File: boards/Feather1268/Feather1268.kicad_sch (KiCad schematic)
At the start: 22 parts, among them J2 USB4105-GF-A, J4 Conn_01x03, U2 ESP32-S3-MINI-1U, U3 ECMF02-2AMX6, U5 AMS1117-3.3

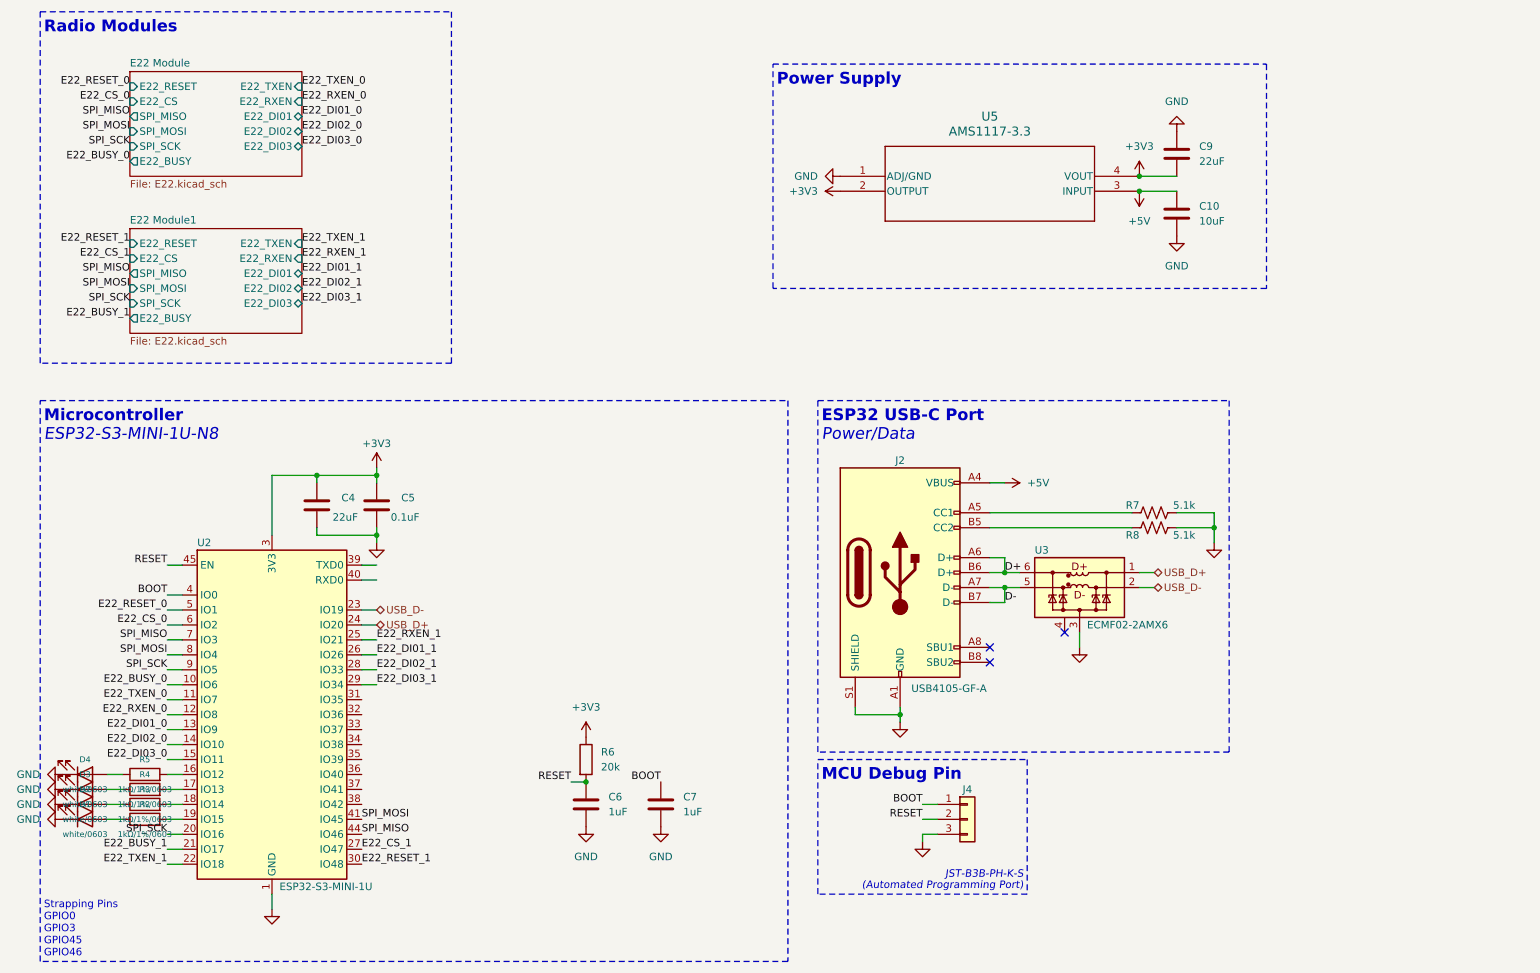
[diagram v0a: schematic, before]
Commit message: made some sch formatting / libs / routing changes
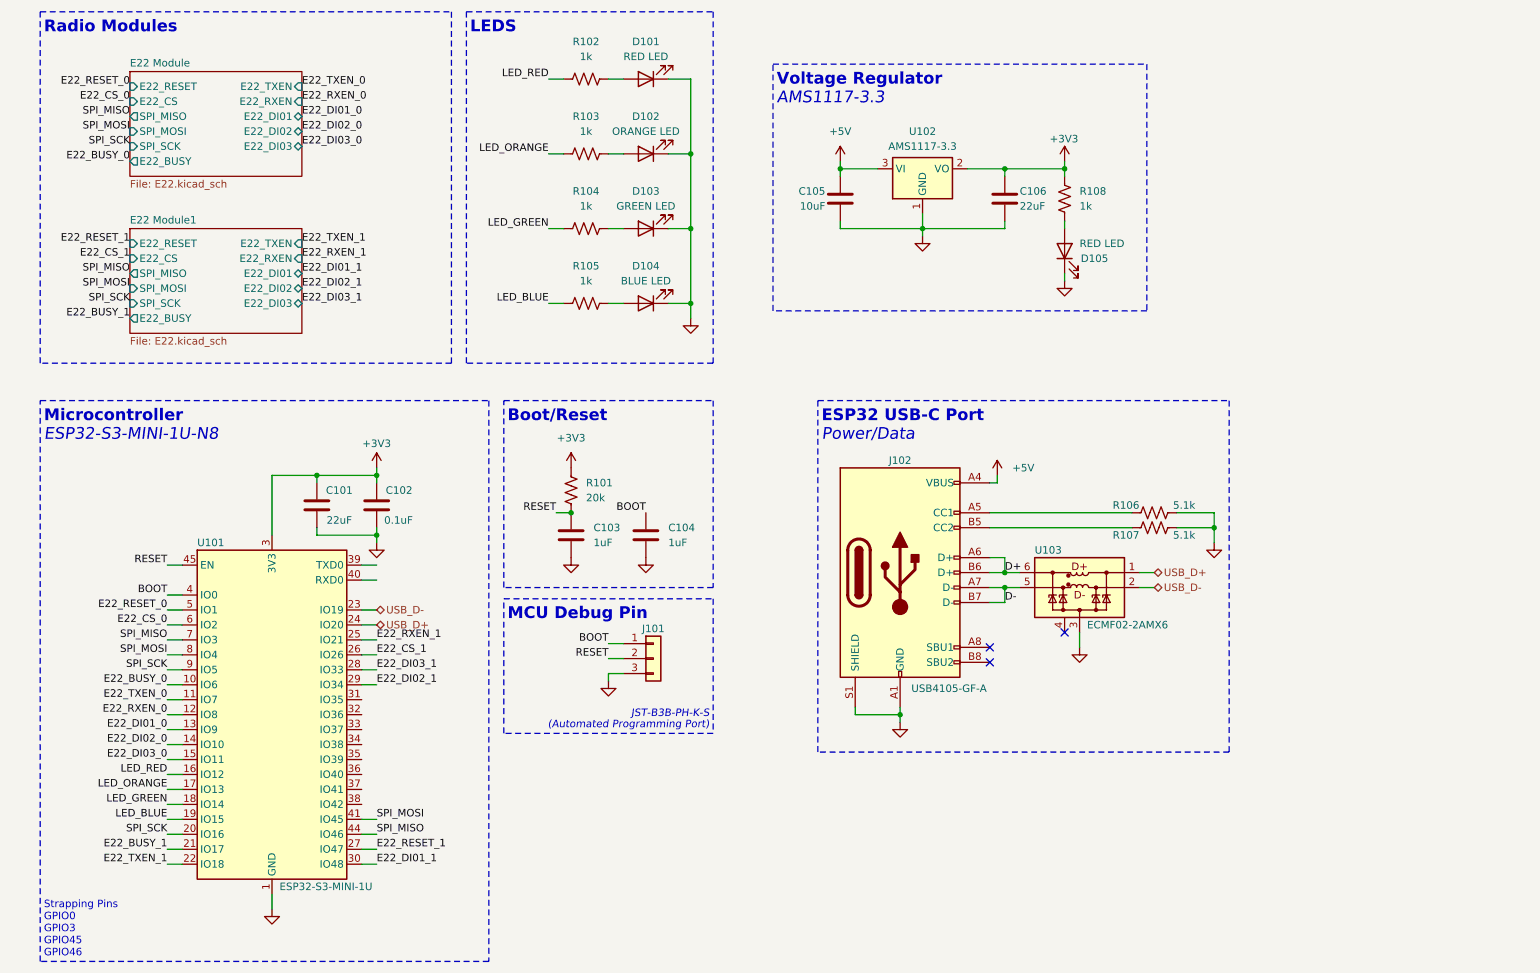
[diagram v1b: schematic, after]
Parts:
- removed C10: 10uF, Capacitor_SMD:C_0603_1608Metric, symbol Device:C
- removed C6, C7: 1uF, Capacitor_SMD:C_0603_1608Metric, symbol Device:C
- removed C9: 22uF, Capacitor_SMD:C_0603_1608Metric, symbol Device:C
- removed D1, D2, D3, D4: white/0603, LED_SMD:LED_0603_1608Metric, symbol Device:LED
- removed R2, R3, R4, R5: 1kΩ/1%/0603, Resistor_SMD:R_0603_1608Metric, symbol TMC2209-BOB-v1.0-rescue:R-Device
- removed R6: 20k, Resistor_SMD:R_0603_1608Metric, symbol Device:R
- removed U5: AMS1117-3.3, SOT_AMS1117-2.5_AMS, symbol AMS1117-3.3:AMS1117-3.3
- added C103, C104: 1uF, Capacitor_SMD:C_0603_1608Metric, symbol Device:C
- added C105: 10uF, Capacitor_SMD:C_0603_1608Metric, symbol Device:C
- added C106: 22uF, Capacitor_SMD:C_0603_1608Metric, symbol Device:C
- added D101, D105: RED LED, LED_SMD:LED_0603_1608Metric, symbol Device:LED
- added D102: ORANGE LED, LED_SMD:LED_0603_1608Metric, symbol Device:LED
- added D103: GREEN LED, LED_SMD:LED_0603_1608Metric, symbol Device:LED
- added D104: BLUE LED, LED_SMD:LED_0603_1608Metric, symbol Device:LED
- added R101: 20k, Resistor_SMD:R_0603_1608Metric, symbol Device:R_US
- added R102, R103, R104, R105, R108: 1k, Resistor_SMD:R_0603_1608Metric, symbol Device:R_US
- added U102: AMS1117-3.3, Package_TO_SOT_SMD:SOT-223-3_TabPin2, symbol Regulator_Linear:AMS1117-3.3
- renumbered C4 to C101, C5 to C102, J4 to J101, J2 to J102, R7 to R106, R8 to R107, U2 to U101, U3 to U103
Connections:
- net +3V3: now also C106.1, R101.1, R108.1, U102.2 (VO)
- net +5V: now also C105.1, U102.3 (VI)
- net BOOT: now also C104.1
- net E22_CS_1: now also U101.26 (IO26); no longer U101.27 (IO47)
- net E22_DI01_1: now also U101.30 (IO48); no longer U101.26 (IO26)
- net E22_DI02_1: now also U101.29 (IO34); no longer U101.28 (IO33)
- net E22_DI03_1: now also U101.28 (IO33); no longer U101.29 (IO34)
- net E22_RESET_1: now also U101.27 (IO47); no longer U101.30 (IO48)
- net GND: now also C103.2, C104.2, C105.2, C106.2, D101.1 (K), D102.1 (K), D103.1 (K), D104.1 (K), D105.1 (K), U102.1 (GND)
- net RESET: now also C103.1, R101.2
- net LED_GREEN: now reaches U101.18 (IO14)
- net LED_GREEN: now also R104.1
- net LED_RED: now reaches U101.16 (IO12)
- net LED_RED: now also R102.1
- net LED_ORANGE: now reaches U101.17 (IO13)
- net LED_ORANGE: now also R103.1
- net LED_BLUE: now reaches U101.19 (IO15)
- net LED_BLUE: now also R105.1
- new net: D105.2 (A), R108.2
- new net: D104.2 (A), R105.2
- new net: D102.2 (A), R103.2
- new net: D103.2 (A), R104.2
- new net: D101.2 (A), R102.2
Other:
- note added: "AMS1117-3.3"
- note added: "Boot/Reset"
- note added: "LEDS"
- note added: "Voltage Regulator"
- note removed: "Power Supply"
- moved on the sheet: J101

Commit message: done ish
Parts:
- added J1: Conn_01x02, Connector_PinHeader_2.54mm:PinHeader_1x02_P2.54mm_Vertical, symbol Connector_Generic:Conn_01x02
- added TP1, TP2, TP3, TP4, TP5, TP6: TestPoint_Small, TestPoint:TestPoint_Pad_D1.0mm, symbol Connector:TestPoint_Small
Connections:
- net E22_BUSY_1: now also U101.22 (IO18); no longer U101.21 (IO17)
- net E22_CS_0: now also U101.5 (IO1); no longer U101.6 (IO2)
- net E22_CS_1: now also U101.21 (IO17); no longer U101.26 (IO26)
- net E22_DI01_0: now also U101.9 (IO5); no longer U101.13 (IO9)
- net E22_DI02_0: now also U101.38 (IO42); no longer U101.14 (IO10)
- net E22_DI03_0: now also U101.41 (IO45); no longer U101.15 (IO11)
- net E22_RESET_0: now also U101.13 (IO9); no longer U101.5 (IO1)
- net E22_RXEN_0: now also U101.11 (IO7); no longer U101.12 (IO8)
- net E22_TXEN_0: now also U101.12 (IO8); no longer U101.11 (IO7)
- net E22_TXEN_1: now also U101.26 (IO26); no longer U101.22 (IO18)
- net at U101.31 (IO35): now also TP1.1
- net at U101.32 (IO36): now also TP2.1
- net at U101.33 (IO37): now also TP3.1
- net at U101.34 (IO38): now also TP4.1
- net at U101.35 (IO39): now also TP5.1
- net at U101.36 (IO40): now also TP6.1
- net TX: now reaches U101.39 (TXD0)
- net TX: now also J1.1 (Pin_1)
- net RX: now reaches U101.40 (RXD0)
- net RX: now also J1.2 (Pin_2)
- net SPI_MISO: no longer names the net of U101.44 (IO46)
- net SPI_MISO: no longer U101.7 (IO3)
- net SPI_MOSI renamed SPI_SCK_0
- net SPI_SCK_0: no longer U101.41 (IO45)
- net SPI_SCK renamed SPI_SCK_1
- net SPI_SCK_1: no longer U101.9 (IO5)
- new net SPI_MISO_0: U101.6 (IO2)
- new net SPI_MISO_1: U101.14 (IO10)
- new net SPI_MOSI_0: U101.7 (IO3)
- new net SPI_MOSI_1: U101.15 (IO11)

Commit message: bigger board
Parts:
- removed J1: Conn_01x02, Connector_PinHeader_2.54mm:PinHeader_1x02_P2.54mm_Vertical, symbol Connector_Generic:Conn_01x02
- removed TP1, TP2, TP3, TP4, TP5, TP6: TestPoint_Small, TestPoint:TestPoint_Pad_D1.0mm, symbol Connector:TestPoint_Small
- added H1, H2, H3: M3, MountingHole:MountingHole_3.2mm_M3_Pad_Via, symbol Mechanical:MountingHole_Pad
- added J1, J2, J3, J4, J5: Conn_01x04, Connector_PinHeader_2.54mm:PinHeader_1x04_P2.54mm_Vertical, symbol Connector_Generic:Conn_01x04
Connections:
- net +3V3: now also J1.4 (Pin_4), J2.4 (Pin_4), J3.4 (Pin_4), J4.4 (Pin_4), J5.4 (Pin_4)
- net E22_BUSY_0: now also U101.5 (IO1); no longer U101.10 (IO6)
- net E22_CS_0: now also U101.8 (IO4); no longer U101.5 (IO1)
- net E22_DI01_0: now also U101.10 (IO6); no longer U101.9 (IO5)
- net GND: now also J1.3 (Pin_3), J2.3 (Pin_3), J3.3 (Pin_3), J4.3 (Pin_3), J5.3 (Pin_3)
- net RX: now also J1.2 (Pin_2)
- net SPI_SCK_0: now also U101.9 (IO5); no longer U101.8 (IO4)
- net TX: now also J1.1 (Pin_1)
- net IO38: now reaches U101.34 (IO38)
- net IO38: now also J3.2 (Pin_2)
- net IO35: now reaches U101.31 (IO35)
- net IO35: now also J2.1 (Pin_1)
- net IO36: now reaches U101.32 (IO36)
- net IO36: now also J2.2 (Pin_2)
- net IO37: now reaches U101.33 (IO37)
- net IO37: now also J3.1 (Pin_1)
- net IO39: now reaches U101.35 (IO39)
- net IO39: now also J4.1 (Pin_1)
- net IO40: now reaches U101.36 (IO40)
- net IO40: now also J4.2 (Pin_2)
- net IO41: now reaches U101.37 (IO41)
- net IO41: now also J5.1 (Pin_1)
- net IO46: now reaches U101.44 (IO46)
- net IO46: now also J5.2 (Pin_2)
- no-connect marks 3 -> 6
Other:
- note added: "Electrically isolated!"
- note added: "Mounting Holes"

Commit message: minor cleanup
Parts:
- renumbered H1 to H101, H2 to H102, H3 to H103, J2 to J101, J3 to J102, J101 to J103, J4 to J104, J5 to J105, J102 to J106, J1 to J107, U103 to U102, U102 to U103
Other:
- note added: "Extra GPIO"
- moved on the sheet: C101, C102, C103, C104, C105, C106, D105, H101, H102, H103, J101, J102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

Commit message: some final changes
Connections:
- net LED_BLUE: now also U101.16 (IO12); no longer U101.19 (IO15)
- net LED_GREEN: now also U101.17 (IO13); no longer U101.18 (IO14)
- net LED_ORANGE: now also U101.18 (IO14); no longer U101.17 (IO13)
- net LED_RED: now also U101.19 (IO15); no longer U101.16 (IO12)
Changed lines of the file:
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@@
 	)
 	(label "LED_BLUE"
-		(at 36.83 148.59 180)
+		(at 36.83 140.97 180)
 		(fields_autoplaced yes)
 		(effects
@@
 	)
 	(label "LED_GREEN"
-		(at 36.83 146.05 180)
+		(at 36.83 143.51 180)
 		(fields_autoplaced yes)
 		(effects
@@
 	)
 	(label "LED_ORANGE"
-		(at 36.83 143.51 180)
+		(at 36.83 146.05 180)
 		(fields_autoplaced yes)
 		(effects
@@
 	)
 	(label "LED_RED"
-		(at 36.83 140.97 180)
-		(fields_autoplaced yes)
-		(effects
+		(at 36.83 148.59 180)
+		(fields_autoplaced yes)
+		(effects
